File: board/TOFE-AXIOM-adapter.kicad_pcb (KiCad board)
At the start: 2 copper layers, 68.9 x 28.3 mm, 11 parts, among them CN1 C, U1 24AA01/24LC01B

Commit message: Small fix.
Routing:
- net /S_IO2: track 39.3 -> 49.0 mm
- net /S_LVDS_4_N: track 25.0 -> 24.1 mm

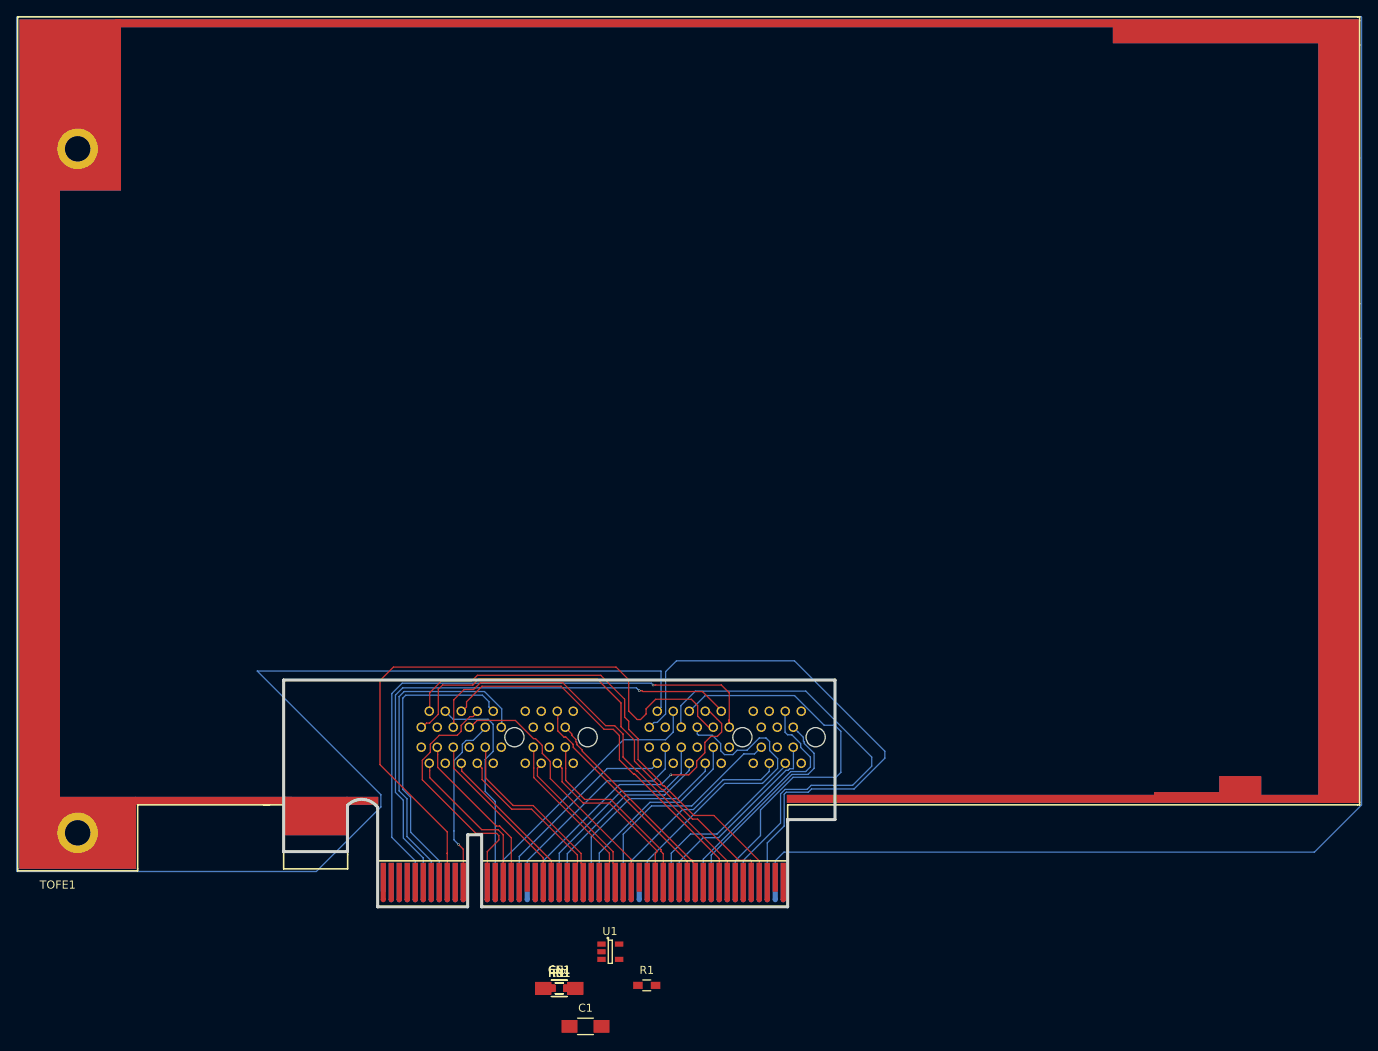
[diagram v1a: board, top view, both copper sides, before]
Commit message: Converted to just the pins footprint.
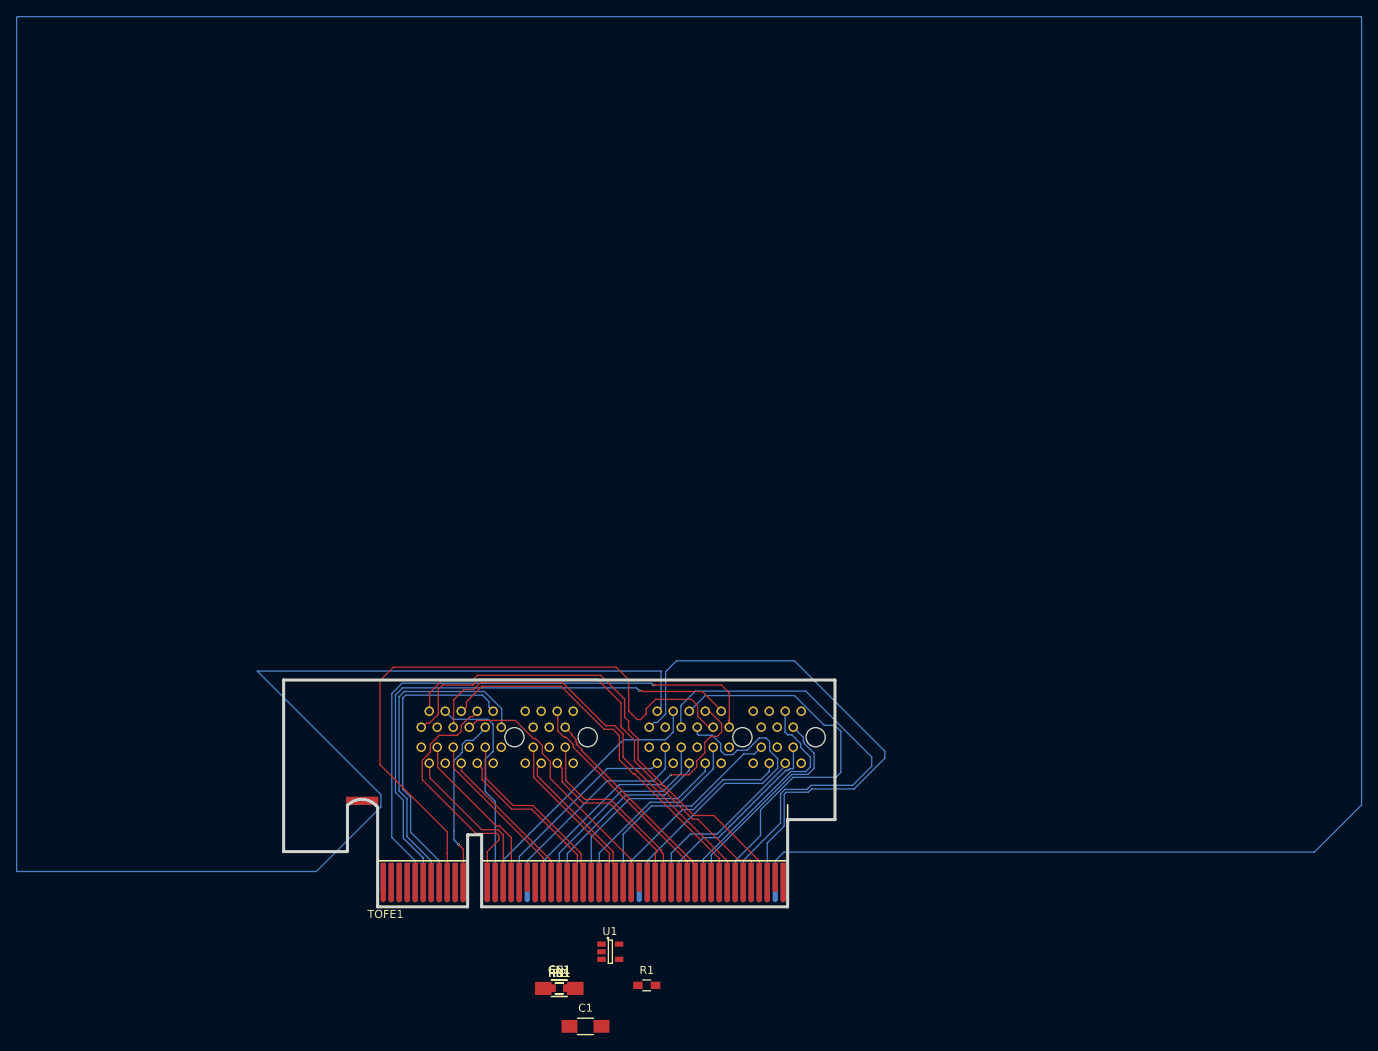
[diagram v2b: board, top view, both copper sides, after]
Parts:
- TOFE1: footprint TOFE_8X_HalfHeight:TOFE_8X_HalfHeight -> TOFE_8X_Pins:TOFE_8X_Pins
- moved TOFE1 45.2 mm to (174.0, 188.2)
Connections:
- NORTH1 pad B13: Net-(NORTH1-PadB13) -> /VCC_3V3
- SOUTH1 pad B13: Net-(SOUTH1-PadB13) -> /VCC_3V3

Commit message: Lots of fix ups.
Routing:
- net /S_SCL: track 580.1 -> 51.4 mm
- net /S_SDA: track 67.7 -> 53.3 mm
- net /S_IO1: track 57.6 -> 50.0 mm
- net /S_IO5: track 79.6 -> 72.7 mm
- net /S_IO2: track 49.0 -> 46.1 mm
- added copper zone on B.Cu, net (none)
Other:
- copper layers 2 -> 4

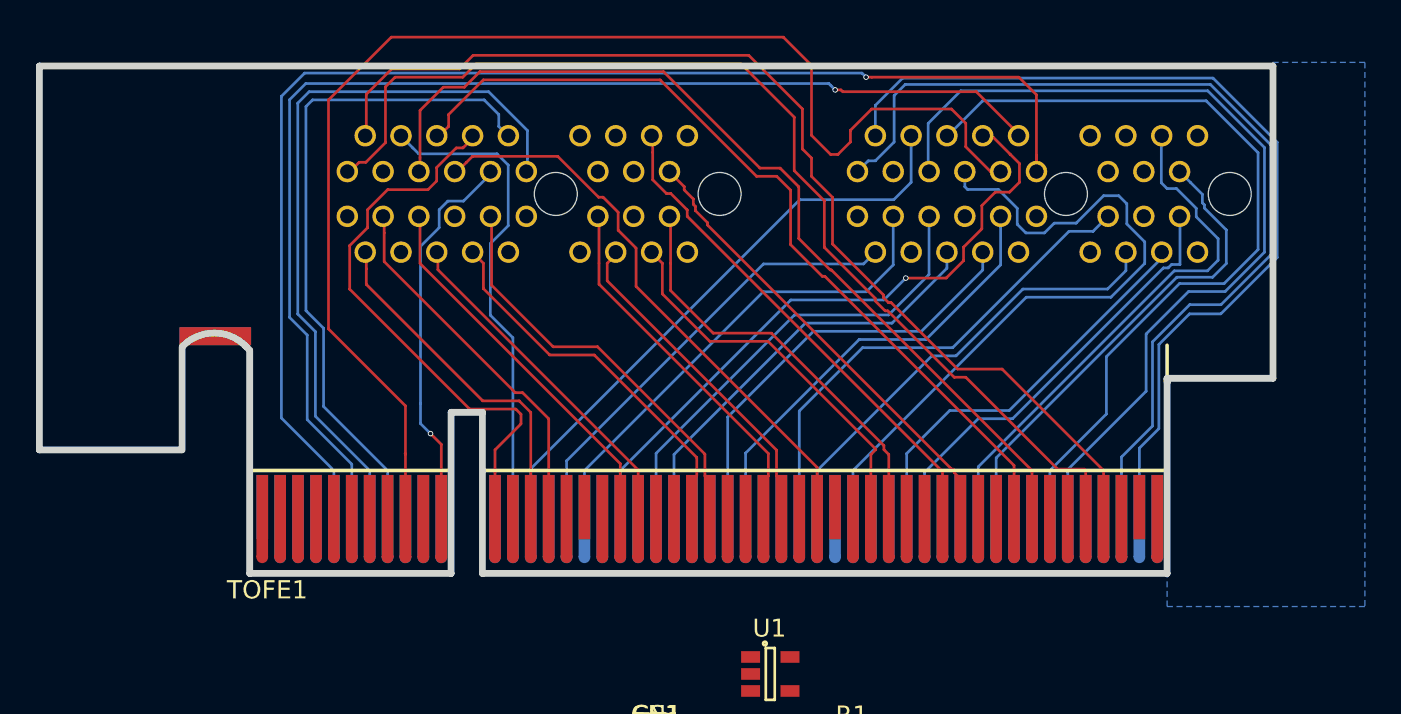
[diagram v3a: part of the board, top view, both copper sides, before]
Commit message: Adding a boundry trace to make the push/shove stuff easier to work with.
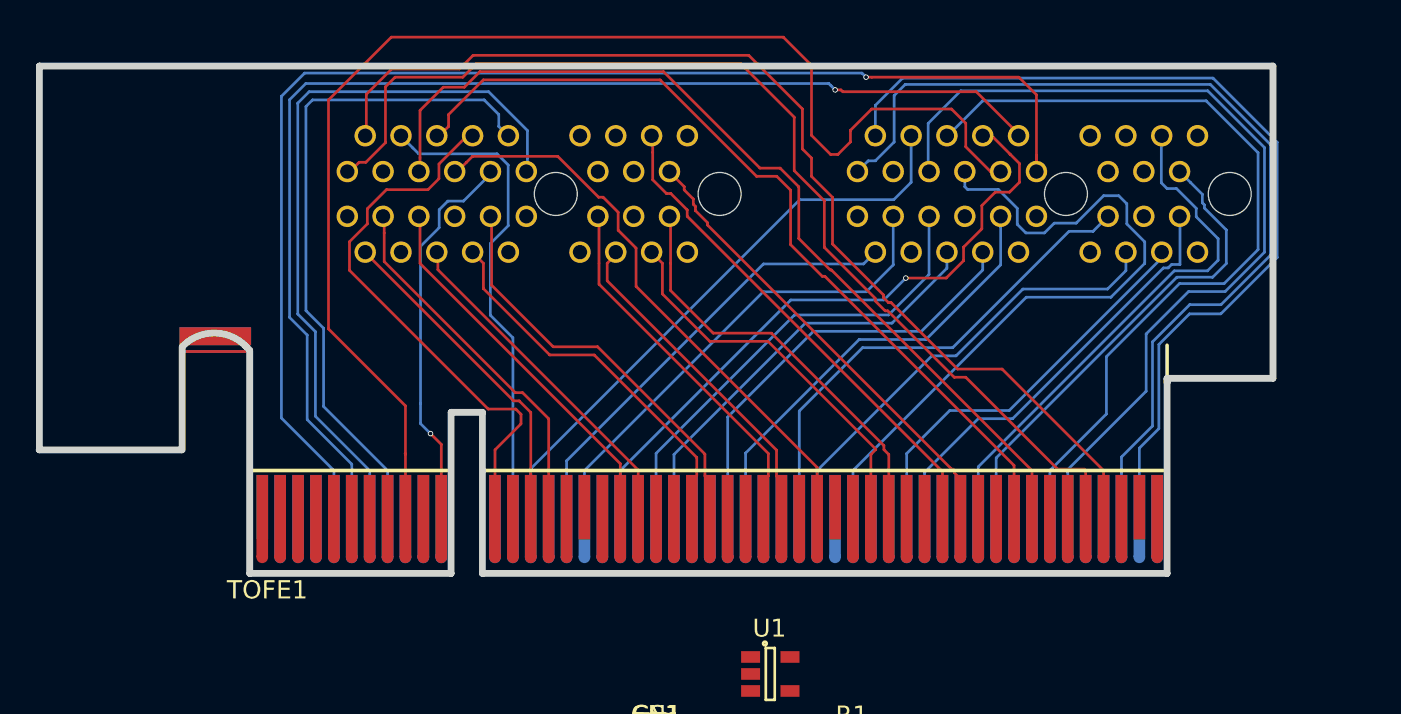
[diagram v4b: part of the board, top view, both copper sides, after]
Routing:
- net (no net): track 0.00 -> 231.6 mm, vias 0 -> 1
- net /N_LVDS_0_P: track 19.7 -> 18.7 mm
- net /N_IO4: track 31.7 -> 31.1 mm
- removed copper zone on B.Cu, net (none)
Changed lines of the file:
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@@
     (thickness 1.6)
     (drawings 25)
-    (tracks 453)
+    (tracks 484)
     (zones 0)
     (modules 11)
@@
   (gr_line (start 225.25 177.25) (end 225.25 188.15) (angle 90) (layer Edge.Cuts) (width 0.381))
   (gr_arc (start 172.01524 177.1926) (end 170.26524 175.4426) (angle 91) (layer Edge.Cuts) (width 0.381))
+  (segment (start 231.15 177.2) (end 225.306682 177.2) (width 0.1524) (layer F.Cu) (net 0))
+  (segment (start 225.306682 177.2) (end 225.303341 177.203341) (width 0.1524) (layer F.Cu) (net 0))
+  (segment (start 187 179.15) (end 185.307442 179.15) (width 0.1524) (layer F.Cu) (net 0))
+  (segment (start 185.307442 179.15) (end 185.303721 179.153721) (width 0.1524) (layer F.Cu) (net 0))
+  (segment (start 225.303341 177.203341) (end 225.303341 188.096659) (width 0.1524) (layer F.Cu) (net 0))
+  (segment (start 225.303341 188.096659) (end 225.25 188.15) (width 0.1524) (layer F.Cu) (net 0))
+  (segment (start 225.25 188.15) (end 187 188.15) (width 0.1524) (layer F.Cu) (net 0))
+  (segment (start 187 188.15) (end 187 179.15) (width 0.1524) (layer F.Cu) (net 0))
+  (segment (start 185.303721 179.153721) (end 185.303721 188.096279) (width 0.1524) (layer F.Cu) (net 0))
+  (segment (start 185.303721 188.096279) (end 185.25 188.15) (width 0.1524) (layer F.Cu) (net 0))
+  (segment (start 185.25 188.15) (end 174 188.15) (width 0.1524) (layer F.Cu) (net 0))
+  (segment (start 174 188.15) (end 174 175.75) (width 0.1524) (layer F.Cu) (net 0))
+  (segment (start 174 175.75) (end 170.2 175.75) (width 0.1524) (layer F.Cu) (net 0))
+  (segment (start 170.2 175.75) (end 170.2 181.25) (width 0.1524) (layer F.Cu) (net 0))
+  (segment (start 170.2 181.25) (end 162.2 181.25) (width 0.1524) (layer F.Cu) (net 0))
+  (via (at 162.2 181.25) (size 0.3048) (drill 0.2032) (layers F.Cu B.Cu) (net 0))
+  (segment (start 170.2 181.25) (end 162.2 181.25) (width 0.1524) (layer B.Cu) (net 0))
+  (segment (start 170.2 175.75) (end 170.2 181.25) (width 0.1524) (layer B.Cu) (net 0))
+  (segment (start 172.2723 175.75) (end 170.2 175.75) (width 0.1524) (layer B.Cu) (net 0))
+  (segment (start 174 175.75) (end 172.2723 175.75) (width 0.1524) (layer B.Cu) (net 0))
+  (segment (start 174 185.75) (end 174 175.75) (width 0.1524) (layer B.Cu) (net 0))
+  (segment (start 174 188.15) (end 174 185.75) (width 0.1524) (layer B.Cu) (net 0))
+  (segment (start 185.3 188.15) (end 174 188.15) (width 0.1524) (layer B.Cu) (net 0))
+  (segment (start 185.3 188.15) (end 185.303721 188.146279) (width 0.1524) (layer B.Cu) (net 0))
+  (segment (start 185.303721 188.146279) (end 185.303721 179.153721) (width 0.1524) (layer B.Cu) (net 0))
+  (segment (start 185.307442 179.15) (end 187 179.15) (width 0.1524) (layer B.Cu) (net 0))
+  (segment (start 185.303721 179.153721) (end 185.307442 179.15) (width 0.1524) (layer B.Cu) (net 0))
+  (segment (start 187 179.15) (end 187 188.15) (width 0.1524) (layer B.Cu) (net 0))
+  (segment (start 187 188.15) (end 225.25 188.15) (width 0.1524) (layer B.Cu) (net 0))
+  (segment (start 225.25 188.15) (end 225.303341 188.096659) (width 0.1524) (layer B.Cu) (net 0))
+  (segment (start 225.303341 188.096659) (end 225.303341 177.203341) (width 0.1524) (layer B.Cu) (net 0))
+  (segment (start 225.303341 177.203341) (end 225.306682 177.2) (width 0.1524) (layer B.Cu) (net 0))
+  (segment (start 225.306682 177.2) (end 231.15 177.2) (width 0.1524) (layer B.Cu) (net 0))
+  (segment (start 231.15 177.2) (end 231.15 177.3) (width 0.1524) (layer B.Cu) (net 0))
   (segment (start 174.7324 187.27524) (end 174.7324 184.974) (width 0.1524) (layer F.Cu) (net 3))
   (segment (start 215.9484 165.70032) (end 215.38526 165.70032) (width 0.1524) (layer F.Cu) (net 8))
@@
   (segment (start 182.69966 184.95518) (end 182.69966 181.48046) (width 0.1524) (layer F.Cu) (net 8))
   (segment (start 182.69966 181.48046) (end 182.6768 181.4576) (width 0.1524) (layer F.Cu) (net 8))
+  (segment (start 186.069854 163.7792) (end 186.5122 163.7792) (width 0.1524) (layer F.Cu) (net 9))
+  (segment (start 184.570579 165.278475) (end 186.069854 163.7792) (width 0.1524) (layer F.Cu) (net 9))
+  (segment (start 184.570579 166.098471) (end 184.570579 165.278475) (width 0.1524) (layer F.Cu) (net 9))
+  (segment (start 180.570079 167.777835) (end 181.637553 166.710361) (width 0.1524) (layer F.Cu) (net 9))
+  (segment (start 181.637553 166.710361) (end 183.958689 166.710361) (width 0.1524) (layer F.Cu) (net 9))
+  (segment (start 179.571859 169.619745) (end 180.570079 168.621525) (width 0.1524) (layer F.Cu) (net 9))
+  (segment (start 187.320035 178.967126) (end 179.571859 171.21895) (width 0.1524) (layer F.Cu) (net 9))
   (segment (start 187.70092 184.95518) (end 187.70092 181.248654) (width 0.1524) (layer F.Cu) (net 9))
   (segment (start 189.15542 179.257702) (end 188.864844 178.967126) (width 0.1524) (layer F.Cu) (net 9))
+  (segment (start 179.571859 171.21895) (end 179.571859 169.619745) (width 0.1524) (layer F.Cu) (net 9))
   (segment (start 187.70092 181.248654) (end 189.15542 179.794154) (width 0.1524) (layer F.Cu) (net 9))
   (segment (start 189.15542 179.794154) (end 189.15542 179.257702) (width 0.1524) (layer F.Cu) (net 9))
-  (segment (start 179.583079 172.267879) (end 179.583079 169.835371) (width 0.1524) (layer F.Cu) (net 9))
-  (segment (start 183.958689 166.710361) (end 184.442101 166.226949) (width 0.1524) (layer F.Cu) (net 9))
-  (segment (start 188.864844 178.967126) (end 186.282326 178.967126) (width 0.1524) (layer F.Cu) (net 9))
-  (segment (start 186.282326 178.967126) (end 179.583079 172.267879) (width 0.1524) (layer F.Cu) (net 9))
-  (segment (start 179.583079 169.835371) (end 180.581299 168.837151) (width 0.1524) (layer F.Cu) (net 9))
-  (segment (start 180.581299 168.837151) (end 180.581299 167.833851) (width 0.1524) (layer F.Cu) (net 9))
-  (segment (start 180.581299 167.833851) (end 181.704789 166.710361) (width 0.1524) (layer F.Cu) (net 9))
-  (segment (start 181.704789 166.710361) (end 183.958689 166.710361) (width 0.1524) (layer F.Cu) (net 9))
-  (segment (start 184.442101 166.226949) (end 184.442101 165.474189) (width 0.1524) (layer F.Cu) (net 9))
-  (segment (start 184.442101 165.474189) (end 185.537651 164.378639) (width 0.1524) (layer F.Cu) (net 9))
-  (segment (start 185.537651 164.378639) (end 185.912761 164.378639) (width 0.1524) (layer F.Cu) (net 9))
-  (segment (start 185.912761 164.378639) (end 186.5122 163.7792) (width 0.1524) (layer F.Cu) (net 9))
+  (segment (start 180.570079 168.621525) (end 180.570079 167.777835) (width 0.1524) (layer F.Cu) (net 9))
+  (segment (start 183.958689 166.710361) (end 184.570579 166.098471) (width 0.1524) (layer F.Cu) (net 9))
+  (segment (start 188.864844 178.967126) (end 187.320035 178.967126) (width 0.1524) (layer F.Cu) (net 9))
   (segment (start 217.95 165.33854) (end 217.95 164.8) (width 0.1524) (layer F.Cu) (net 10))
   (segment (start 217.95 164.8) (end 217.95 161.4096) (width 0.1524) (layer F.Cu) (net 10))
@@
   (segment (start 181.51094 170.726436) (end 181.51094 169.127816) (width 0.1524) (layer F.Cu) (net 44))
   (segment (start 181.51094 169.127816) (end 181.51094 168.28008) (width 0.1524) (layer F.Cu) (net 44))
-  (segment (start 180.51272 172.005935) (end 180.51272 171.129336) (width 0.1524) (layer F.Cu) (net 45))
+  (segment (start 189.054226 178.509915) (end 188.741035 178.509915) (width 0.1524) (layer F.Cu) (net 45))
+  (segment (start 188.741035 178.509915) (end 180.51272 170.2816) (width 0.1524) (layer F.Cu) (net 45))
   (segment (start 189.6999 184.95518) (end 189.6999 179.155589) (width 0.1524) (layer F.Cu) (net 45))
-  (segment (start 189.054226 178.509915) (end 187.0167 178.509915) (width 0.1524) (layer F.Cu) (net 45))
-  (segment (start 187.0167 178.509915) (end 180.51272 172.005935) (width 0.1524) (layer F.Cu) (net 45))
   (segment (start 189.6999 179.155589) (end 189.054226 178.509915) (width 0.1524) (layer F.Cu) (net 45))
-  (segment (start 180.51272 171.129336) (end 180.51272 170.2816) (width 0.1524) (layer F.Cu) (net 45))
   (segment (start 184.51068 170.2816) (end 184.51068 171.182575) (width 0.1524) (layer F.Cu) (net 46))
   (segment (start 184.51068 171.182575) (end 195.7008 182.372695) (width 0.1524) (layer F.Cu) (net 46))
@@
   (segment (start 227.794204 171.602389) (end 228.557211 170.839382) (width 0.1524) (layer B.Cu) (net 59))
   (segment (start 215.7008 184.95518) (end 215.7008 181.696286) (width 0.1524) (layer B.Cu) (net 59))
-  (zone (net 0) (net_name "") (layer B.Cu) (hatch full 0.508)
-    (connect_pads (clearance 0.127))
-    (min_thickness 0.254)
-    (fill yes (arc_segments 16) (thermal_gap 0.508) (thermal_bridge_width 0.508))
-    (polygon
-      (pts
-        (xy 225.25 177.2) (xy 231.15 177.2) (xy 231.15 159.6) (xy 236.3 159.6) (xy 236.3 190)
-        (xy 225.25 190)
-      )
-    )
-  )
 )

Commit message: More routing.
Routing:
- net /S_IO5: track 72.7 -> 67.0 mm
- net /VCC12V: track 2.30 -> 0.00 mm
- net /N_IO4: track 31.1 -> 29.2 mm
- net /N_LVDS_1_N: track 19.3 -> 20.3 mm
- net /N_LVDS_0_P: track 18.7 -> 19.3 mm
- net /N_SDA: track 61.2 -> 60.6 mm
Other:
- net class Default: clearance 0.2032 -> 0.1524
- rule trace_clearance: 0.2032 -> 0.1524
